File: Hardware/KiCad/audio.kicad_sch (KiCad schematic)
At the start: 36 parts, among them IC1 LM4861M, J4 Kenwood-3.5, J5 Kenwood-2.5, SW1 SW_Push, U5 MAX9814

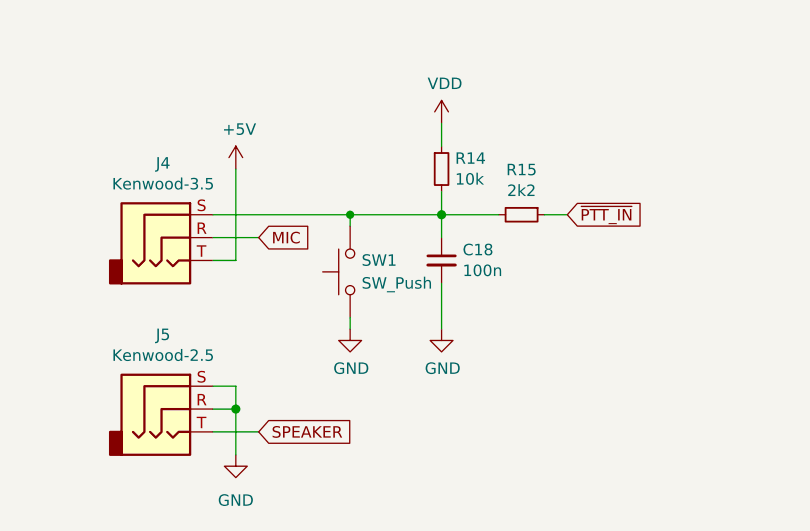
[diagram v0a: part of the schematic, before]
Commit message: Added footprints for decoupling caps
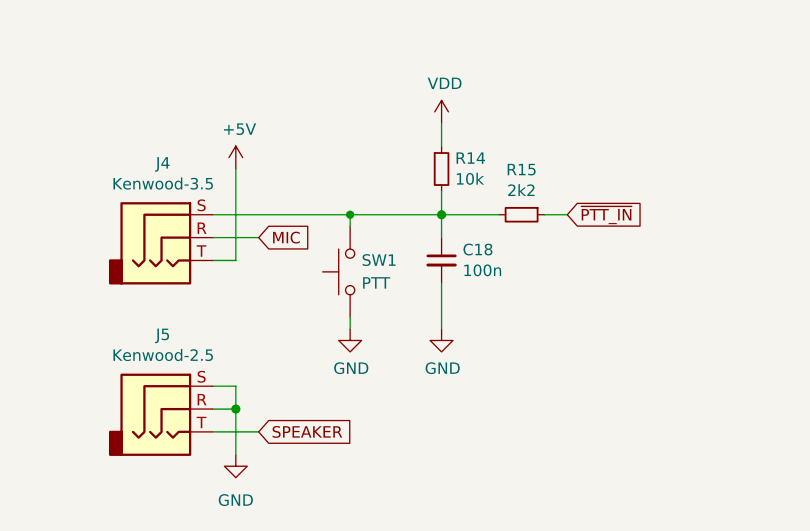
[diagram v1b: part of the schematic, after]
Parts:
- SW1: value SW_Push -> PTT; footprint (none) -> Button_Switch_THT:SW_Tactile_SPST_Angled_PTS645Vx31-2LFS
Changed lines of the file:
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@@
       (effects (font (size 1.27 1.27)) (justify right))
     )
-    (property "Value" "SW_Push" (id 1) (at 62.23 135.8899 90)
+    (property "Value" "PTT" (id 1) (at 62.23 135.8899 90)
       (effects (font (size 1.27 1.27)) (justify right))
     )
-    (property "Footprint" "" (id 2) (at 55.88 134.62 0)
+    (property "Footprint" "Button_Switch_THT:SW_Tactile_SPST_Angled_PTS645Vx31-2LFS" (id 2) (at 55.88 134.62 0)
       (effects (font (size 1.27 1.27)) hide)
     )

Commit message: Initial PCB arrangement
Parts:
- MK1: footprint (none) -> Connector_PinSocket_2.54mm:PinSocket_2x01_P2.54mm_Vertical
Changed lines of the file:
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@@
       (effects (font (size 1.27 1.27)) (justify left))
     )
-    (property "Footprint" "" (id 2) (at 24.13 82.55 90)
+    (property "Footprint" "Connector_PinSocket_2.54mm:PinSocket_2x01_P2.54mm_Vertical" (id 2) (at 24.13 82.55 90)
       (effects (font (size 1.27 1.27)) hide)
     )
